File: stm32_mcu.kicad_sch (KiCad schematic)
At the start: 9 parts, among them J4 Conn_ARM_SWD_TagConnect_TC203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, J5 Conn_01x08_Pin, J6 Conn_01x08_Pin, U1 STM32G031J6Mx

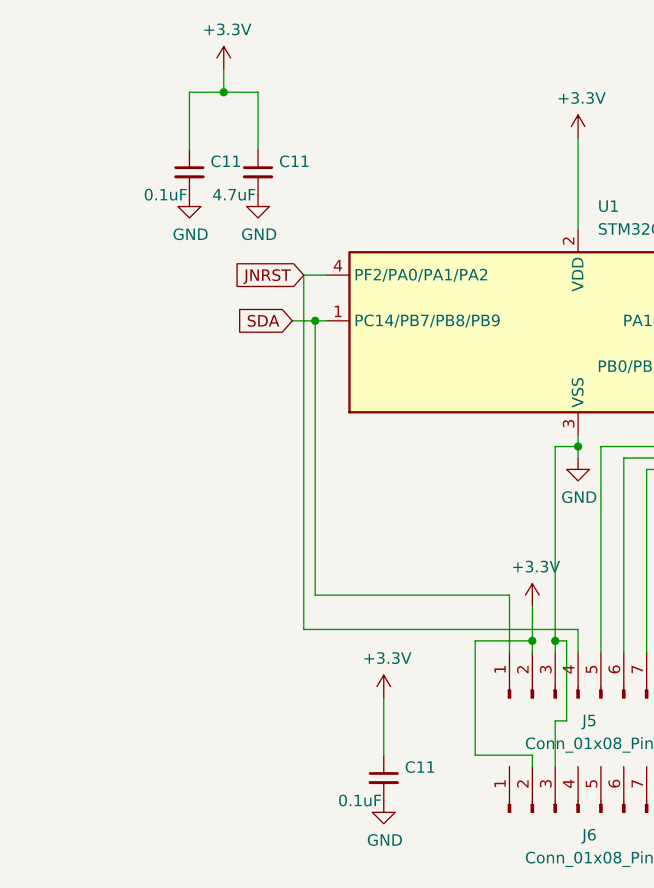
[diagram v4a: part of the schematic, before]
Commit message: Fix decimal point connection on ds4, add info to title block
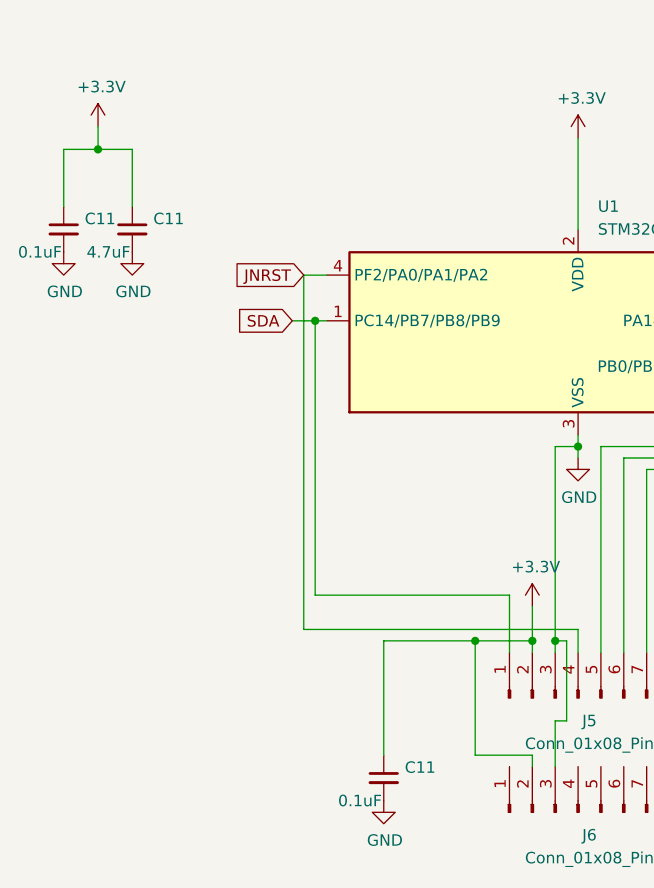
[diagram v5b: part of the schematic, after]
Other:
- company: (none) -> Andrew Tudoroi
- title: (none) -> Pitanga HAT
- moved on the sheet: C11
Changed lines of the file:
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@@
 (kicad_sch (version 20230121) (generator eeschema)
   (paper "A4")
+  (title_block
+    (title "Pitanga HAT")
+    (date "2023-10-19")
+    (rev "2.1")
+    (company "Andrew Tudoroi")
+  )
   (junction (at 149.86 118.11) (diameter 0) (color 0 0 0 0)
   )
@@
   (junction (at 152.4 118.11) (diameter 0) (color 0 0 0 0)
   )
+  (junction (at 143.51 118.11) (diameter 0) (color 0 0 0 0)
+  )
   (junction (at 154.94 96.52) (diameter 0) (color 0 0 0 0)
   )
@@
   (junction (at 184.15 82.55) (diameter 0) (color 0 0 0 0)
   )
-  (junction (at 115.57 57.15) (diameter 0) (color 0 0 0 0)
+  (junction (at 101.6 63.5) (diameter 0) (color 0 0 0 0)
   )
   (wire (pts (xy 123.19 82.55) (xy 125.73 82.55))
@@
     (stroke (width 0) (type default))
   )
-  (wire (pts (xy 119.38 57.15) (xy 119.38 63.5))
+  (wire (pts (xy 105.41 63.5) (xy 105.41 69.85))
     (stroke (width 0) (type default))
   )
@@
     (stroke (width 0) (type default))
   )
-  (wire (pts (xy 133.35 124.46) (xy 133.35 130.81))
+  (wire (pts (xy 133.35 118.11) (xy 133.35 130.81))
     (stroke (width 0) (type default))
   )
@@
     (stroke (width 0) (type default))
   )
-  (wire (pts (xy 111.76 57.15) (xy 111.76 63.5))
+  (wire (pts (xy 97.79 63.5) (xy 97.79 69.85))
     (stroke (width 0) (type default))
   )
@@
     (stroke (width 0) (type default))
   )
+  (wire (pts (xy 133.35 118.11) (xy 143.51 118.11))
+    (stroke (width 0) (type default))
+  )
   (wire (pts (xy 154.94 116.84) (xy 124.46 116.84))
     (stroke (width 0) (type default))
   )
-  (wire (pts (xy 111.76 57.15) (xy 115.57 57.15))
+  (wire (pts (xy 97.79 63.5) (xy 101.6 63.5))
     (stroke (width 0) (type default))
   )
@@
     (stroke (width 0) (type default))
   )
-  (wire (pts (xy 115.57 54.61) (xy 115.57 57.15))
-    (stroke (width 0) (type default))
-  )
-  (wire (pts (xy 119.38 57.15) (xy 115.57 57.15))
+  (wire (pts (xy 101.6 60.96) (xy 101.6 63.5))
+    (stroke (width 0) (type default))
+  )
+  (wire (pts (xy 105.41 63.5) (xy 101.6 63.5))
     (stroke (width 0) (type default))
   )
@@
     )
   )
-  (symbol (lib_id "power:GND") (at 119.38 68.58 0) (unit 1)
-    (in_bom yes) (on_board yes) (dnp no)
-    (property "Reference" "#PWR038" (at 119.38 74.93 0)
-      (effects (font (size 1.27 1.27)) hide)
-    )
-    (property "Value" "GND" (at 119.507 72.9742 0)
-      (effects (font (size 1.27 1.27)))
-    )
-    (property "Footprint" "" (at 119.38 68.58 0)
-      (effects (font (size 1.27 1.27)) hide)
-    )
-    (property "Datasheet" "" (at 119.38 68.58 0)
+  (symbol (lib_id "power:GND") (at 105.41 74.93 0) (unit 1)
+    (in_bom yes) (on_board yes) (dnp no)
+    (property "Reference" "#PWR038" (at 105.41 81.28 0)
+      (effects (font (size 1.27 1.27)) hide)
+    )
+    (property "Value" "GND" (at 105.537 79.3242 0)
+      (effects (font (size 1.27 1.27)))
+    )
+    (property "Footprint" "" (at 105.41 74.93 0)
+      (effects (font (size 1.27 1.27)) hide)
+    )
+    (property "Datasheet" "" (at 105.41 74.93 0)
       (effects (font (size 1.27 1.27)) hide)
     )
@@
         (path "/eed35b77-cbf9-4596-9b17-2558f81058ba/c7f9496d-fb5e-4ce7-92b5-54c2d3a6681a"
           (reference "#PWR028") (unit 1)
-        )
-      )
-    )
-  )
-  (symbol (lib_id "rpi-pico-debugger-shoe-rescue:+3.3V-power") (at 133.35 124.46 0) (unit 1)
-    (in_bom yes) (on_board yes) (dnp no)
-    (property "Reference" "#PWR0104" (at 133.35 128.27 0)
-      (effects (font (size 1.27 1.27)) hide)
-    )
-    (property "Value" "+3.3V" (at 133.731 120.0658 0)
-      (effects (font (size 1.27 1.27)))
-    )
-    (property "Footprint" "" (at 133.35 124.46 0)
-      (effects (font (size 1.27 1.27)) hide)
-    )
-    (property "Datasheet" "" (at 133.35 124.46 0)
-      (effects (font (size 1.27 1.27)) hide)
-    )
-    (pin "1")
-    (instances
-      (project "rpi-pico-debugger-shoe"
-        (path "/aad74d97-f116-4a83-b498-c8cb2f4b4e35"
-          (reference "#PWR0104") (unit 1)
-        )
-      )
-      (project "ltp_kikad"
-        (path "/eed35b77-cbf9-4596-9b17-2558f81058ba"
-          (reference "#PWR0119") (unit 1)
-        )
-        (path "/eed35b77-cbf9-4596-9b17-2558f81058ba/c7f9496d-fb5e-4ce7-92b5-54c2d3a6681a"
-          (reference "#PWR030") (unit 1)
         )
       )
@@
     )
   )
-  (symbol (lib_id "power:GND") (at 111.76 68.58 0) (unit 1)
-    (in_bom yes) (on_board yes) (dnp no)
-    (property "Reference" "#PWR038" (at 111.76 74.93 0)
-      (effects (font (size 1.27 1.27)) hide)
-    )
-    (property "Value" "GND" (at 111.887 72.9742 0)
-      (effects (font (size 1.27 1.27)))
-    )
-    (property "Footprint" "" (at 111.76 68.58 0)
-      (effects (font (size 1.27 1.27)) hide)
-    )
-    (property "Datasheet" "" (at 111.76 68.58 0)
+  (symbol (lib_id "power:GND") (at 97.79 74.93 0) (unit 1)
+    (in_bom yes) (on_board yes) (dnp no)
+    (property "Reference" "#PWR038" (at 97.79 81.28 0)
+      (effects (font (size 1.27 1.27)) hide)
+    )
+    (property "Value" "GND" (at 97.917 79.3242 0)
+      (effects (font (size 1.27 1.27)))
+    )
+    (property "Footprint" "" (at 97.79 74.93 0)
+      (effects (font (size 1.27 1.27)) hide)
+    )
+    (property "Datasheet" "" (at 97.79 74.93 0)
       (effects (font (size 1.27 1.27)) hide)
     )
@@
     )
   )
-  (symbol (lib_id "rpi-pico-debugger-shoe-rescue:+3.3V-power") (at 115.57 54.61 0) (unit 1)
-    (in_bom yes) (on_board yes) (dnp no)
-    (property "Reference" "#PWR0104" (at 115.57 58.42 0)
-      (effects (font (size 1.27 1.27)) hide)
-    )
-    (property "Value" "+3.3V" (at 115.951 50.2158 0)
-      (effects (font (size 1.27 1.27)))
-    )
-    (property "Footprint" "" (at 115.57 54.61 0)
-      (effects (font (size 1.27 1.27)) hide)
-    )
-    (property "Datasheet" "" (at 115.57 54.61 0)
+  (symbol (lib_id "rpi-pico-debugger-shoe-rescue:+3.3V-power") (at 101.6 60.96 0) (unit 1)
+    (in_bom yes) (on_board yes) (dnp no)
+    (property "Reference" "#PWR0104" (at 101.6 64.77 0)
+      (effects (font (size 1.27 1.27)) hide)
+    )
+    (property "Value" "+3.3V" (at 101.981 56.5658 0)
+      (effects (font (size 1.27 1.27)))
+    )
+    (property "Footprint" "" (at 101.6 60.96 0)
+      (effects (font (size 1.27 1.27)) hide)
+    )
+    (property "Datasheet" "" (at 101.6 60.96 0)
       (effects (font (size 1.27 1.27)) hide)
     )
@@
     )
   )
-  (symbol (lib_id "Device:C_Small") (at 119.38 66.04 0) (unit 1)
-    (in_bom yes) (on_board yes) (dnp no)
-    (property "Reference" "C11" (at 121.7168 64.8716 0)
+  (symbol (lib_id "Device:C_Small") (at 105.41 72.39 0) (unit 1)
+    (in_bom yes) (on_board yes) (dnp no)
+    (property "Reference" "C11" (at 107.7468 71.2216 0)
       (effects (font (size 1.27 1.27)) (justify left))
     )
-    (property "Value" "4.7uF" (at 114.3 68.58 0)
+    (property "Value" "4.7uF" (at 100.33 74.93 0)
       (effects (font (size 1.27 1.27)) (justify left))
     )
-    (property "Footprint" "Capacitor_SMD:C_0603_1608Metric" (at 119.38 66.04 0)
-      (effects (font (size 1.27 1.27)) hide)
-    )
-    (property "Datasheet" "~" (at 119.38 66.04 0)
+    (property "Footprint" "Capacitor_SMD:C_0603_1608Metric" (at 105.41 72.39 0)
+      (effects (font (size 1.27 1.27)) hide)
+    )
+    (property "Datasheet" "~" (at 105.41 72.39 0)
       (effects (font (size 1.27 1.27)) hide)
     )
@@
     )
   )
-  (symbol (lib_id "Device:C_Small") (at 111.76 66.04 0) (unit 1)
-    (in_bom yes) (on_board yes) (dnp no)
-    (property "Reference" "C11" (at 114.0968 64.8716 0)
+  (symbol (lib_id "Device:C_Small") (at 97.79 72.39 0) (unit 1)
+    (in_bom yes) (on_board yes) (dnp no)
+    (property "Reference" "C11" (at 100.1268 71.2216 0)
       (effects (font (size 1.27 1.27)) (justify left))
     )
-    (property "Value" "0.1uF" (at 106.68 68.58 0)
+    (property "Value" "0.1uF" (at 92.71 74.93 0)
       (effects (font (size 1.27 1.27)) (justify left))
     )
-    (property "Footprint" "Capacitor_SMD:C_0402_1005Metric" (at 111.76 66.04 0)
-      (effects (font (size 1.27 1.27)) hide)
-    )
-    (property "Datasheet" "~" (at 111.76 66.04 0)
-      (effects (font (size 1.27 1.27)) hide)
-    )
+    (property "Footprint" "Capacitor_SMD:C_0402_1005Metric" (at 97.79 72.39 0)
+      (effects (font (size 1.27 1.27)) hide)
+    )
+    (property "Datasheet" "~" (at 97.79 72.39 0)
+      (effects (font (size 1.27 1.27)) hide)
+    )

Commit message: Piatnag_5_bt
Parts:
- renumbered D3 to D4, J5 to J4, J6 to J5, J4 to J6, U1 to U2
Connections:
- net SDA renamed MCU_SDA
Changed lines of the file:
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@@
     )
   )
-  (global_label "SDA" (shape input) (at 123.19 82.55 180)
+  (global_label "MCU_SDA" (shape input) (at 123.19 82.55 180)
     (effects (font (size 1.27 1.27)) (justify right))
     (property "Intersheetrefs" "${INTERSHEET_REFS}" (at 123.19 82.55 0)
@@
     )
   )
-  (global_label "SCL" (shape input) (at 187.96 82.55 0)
+  (global_label "MCU_SCL" (shape input) (at 187.96 82.55 0)
     (effects (font (size 1.27 1.27)) (justify left))
     (property "Intersheetrefs" "${INTERSHEET_REFS}" (at 194.3734 82.55 0)
@@
         )
         (path "/eed35b77-cbf9-4596-9b17-2558f81058ba/c7f9496d-fb5e-4ce7-92b5-54c2d3a6681a"
-          (reference "#PWR028") (unit 1)
+          (reference "#PWR042") (unit 1)
         )
       )
@@
   (symbol (lib_id "MCU_ST_STM32G0:STM32G031J6Mx") (at 152.4 85.09 0) (unit 1)
     (in_bom yes) (on_board yes) (dnp no) (fields_autoplaced)
-    (property "Reference" "U1" (at 157.1341 69.85 0)
+    (property "Reference" "U2" (at 157.1341 69.85 0)
       (effects (font (size 1.27 1.27)) (justify left))
     )
@@
       (project "ltp_kikad"
         (path "/eed35b77-cbf9-4596-9b17-2558f81058ba/c7f9496d-fb5e-4ce7-92b5-54c2d3a6681a"
-          (reference "U1") (unit 1)
+          (reference "U2") (unit 1)
         )
       )
@@
   (symbol (lib_id "Connector:Conn_01x08_Pin") (at 154.94 124.46 90) (unit 1)
     (in_bom yes) (on_board yes) (dnp no) (fields_autoplaced)
-    (property "Reference" "J5" (at 156.21 127 90)
+    (property "Reference" "J4" (at 156.21 127 90)
       (effects (font (size 1.27 1.27)))
     )
@@
       (project "ltp_kikad"
         (path "/eed35b77-cbf9-4596-9b17-2558f81058ba/c7f9496d-fb5e-4ce7-92b5-54c2d3a6681a"
-          (reference "J5") (unit 1)
+          (reference "J4") (unit 1)
         )
       )
@@
         )
         (path "/eed35b77-cbf9-4596-9b17-2558f81058ba/c7f9496d-fb5e-4ce7-92b5-54c2d3a6681a"
-          (reference "#PWR024") (unit 1)
+          (reference "#PWR048") (unit 1)
         )
       )
@@
         )
         (path "/eed35b77-cbf9-4596-9b17-2558f81058ba/c7f9496d-fb5e-4ce7-92b5-54c2d3a6681a"
-          (reference "#PWR025") (unit 1)
+          (reference "#PWR040") (unit 1)
         )
       )
@@
   (symbol (lib_id "Connector:Conn_01x08_Pin") (at 154.94 137.16 90) (unit 1)
     (in_bom yes) (on_board yes) (dnp no) (fields_autoplaced)
-    (property "Reference" "J6" (at 156.21 139.7 90)
+    (property "Reference" "J5" (at 156.21 139.7 90)
       (effects (font (size 1.27 1.27)))
     )
@@
       (project "ltp_kikad"
         (path "/eed35b77-cbf9-4596-9b17-2558f81058ba/c7f9496d-fb5e-4ce7-92b5-54c2d3a6681a"
-          (reference "J6") (unit 1)
+          (reference "J5") (unit 1)
         )
       )
@@
         )
         (path "/eed35b77-cbf9-4596-9b17-2558f81058ba/c7f9496d-fb5e-4ce7-92b5-54c2d3a6681a"
-          (reference "#PWR031") (unit 1)
+          (reference "#PWR049") (unit 1)
         )
       )
@@
         )
         (path "/eed35b77-cbf9-4596-9b17-2558f81058ba/c7f9496d-fb5e-4ce7-92b5-54c2d3a6681a"
-          (reference "C12") (unit 1)
+          (reference "C15") (unit 1)
         )
       )
@@
         )
         (path "/eed35b77-cbf9-4596-9b17-2558f81058ba/c7f9496d-fb5e-4ce7-92b5-54c2d3a6681a"
-          (reference "#PWR029") (unit 1)
+          (reference "#PWR047") (unit 1)
         )
       )
@@
         )
         (path "/eed35b77-cbf9-4596-9b17-2558f81058ba/c7f9496d-fb5e-4ce7-92b5-54c2d3a6681a"
-          (reference "R10") (unit 1)
+          (reference "R19") (unit 1)
         )
       )
@@
         )
         (path "/eed35b77-cbf9-4596-9b17-2558f81058ba/c7f9496d-fb5e-4ce7-92b5-54c2d3a6681a"
-          (reference "#PWR023") (unit 1)
+          (reference "#PWR041") (unit 1)
         )
       )
@@
         )
         (path "/eed35b77-cbf9-4596-9b17-2558f81058ba/c7f9496d-fb5e-4ce7-92b5-54c2d3a6681a"
-          (reference "C9") (unit 1)
+          (reference "C14") (unit 1)
         )
       )
@@
   (symbol (lib_id "Device:LED") (at 200.66 69.85 180) (unit 1)
     (in_bom yes) (on_board yes) (dnp no) (fields_autoplaced)
-    (property "Reference" "D3" (at 202.2475 62.23 0)
+    (property "Reference" "D4" (at 202.2475 62.23 0)
       (effects (font (size 1.27 1.27)))
     )
@@
       (project "ltp_kikad"
         (path "/eed35b77-cbf9-4596-9b17-2558f81058ba/c7f9496d-fb5e-4ce7-92b5-54c2d3a6681a"
-          (reference "D3") (unit 1)
+          (reference "D4") (unit 1)
         )
       )
@@
   (symbol (lib_id "Connector:Conn_ARM_SWD_TagConnect_TC2030-NL") (at 260.35 81.28 0) (unit 1)
     (in_bom no) (on_board yes) (dnp no) (fields_autoplaced)
-    (property "Reference" "J4" (at 254 80.01 0)
+    (property "Reference" "J6" (at 254 80.01 0)
       (effects (font (size 1.27 1.27)) (justify right))
     )
@@
       (project "ltp_kikad"
         (path "/eed35b77-cbf9-4596-9b17-2558f81058ba/c7f9496d-fb5e-4ce7-92b5-54c2d3a6681a"
-          (reference "J4") (unit 1)
+          (reference "J6") (unit 1)
         )
       )
@@
         )
         (path "/eed35b77-cbf9-4596-9b17-2558f81058ba/c7f9496d-fb5e-4ce7-92b5-54c2d3a6681a"
-          (reference "#PWR027") (unit 1)
+          (reference "#PWR044") (unit 1)
         )
       )
@@
         )
         (path "/eed35b77-cbf9-4596-9b17-2558f81058ba/c7f9496d-fb5e-4ce7-92b5-54c2d3a6681a"
-          (reference "#PWR040") (unit 1)
+          (reference "#PWR043") (unit 1)
         )
       )
@@
         )
         (path "/eed35b77-cbf9-4596-9b17-2558f81058ba/c7f9496d-fb5e-4ce7-92b5-54c2d3a6681a"
-          (reference "#PWR022") (unit 1)
+          (reference "#PWR046") (unit 1)
         )
       )
@@
         )
         (path "/eed35b77-cbf9-4596-9b17-2558f81058ba/c7f9496d-fb5e-4ce7-92b5-54c2d3a6681a"
-          (reference "C7") (unit 1)
+          (reference "C13") (unit 1)
         )
       )
@@
         )
         (path "/eed35b77-cbf9-4596-9b17-2558f81058ba/c7f9496d-fb5e-4ce7-92b5-54c2d3a6681a"
-          (reference "#PWR06") (unit 1)
-        )
-      )
+          (reference "#PWR045") (unit 1)
+        )
+      )

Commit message: Move from 4 layer to 2, complete roting, separate 5v for led driver and 3v i2c power
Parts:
- removed C11 (x2): 0.1uF, Capacitor_SMD:C_0402_1005Metric, symbol Device:C_Small
- removed C11: 4.7uF, Capacitor_SMD:C_0603_1608Metric, symbol Device:C_Small
- removed D4: LED, LED_SMD:LED_0402_1005Metric, symbol Device:LED
- removed J4, J5: Conn_01x08_Pin, Connector_PinHeader_1.00mm:PinHeader_1x08_P1.00mm_Vertical, symbol Connector:Conn_01x08_Pin
- removed J6: Conn_ARM_SWD_TagConnect_TC2030-NL, Connector:Tag-Connect_TC2030-IDC-NL_2x03_P1.27mm_Vertical, symbol Connector:Conn_ARM_SWD_TagConnect_TC2030-NL
- removed R3: 510, Resistor_SMD:R_0402_1005Metric, symbol Device:R
- removed U2: STM32G031J6Mx, Package_SO:SOIC-8_3.9x4.9mm_P1.27mm, symbol MCU_ST_STM32G0:STM32G031J6Mx
